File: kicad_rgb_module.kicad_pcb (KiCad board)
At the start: 2 copper layers, 25 x 25 mm, 41 parts, among them J1 Conn_HackConnect, SW1 TS-1088-AR02016, U1 STM32G030F6P6, U2 NCP114ASN330T1G

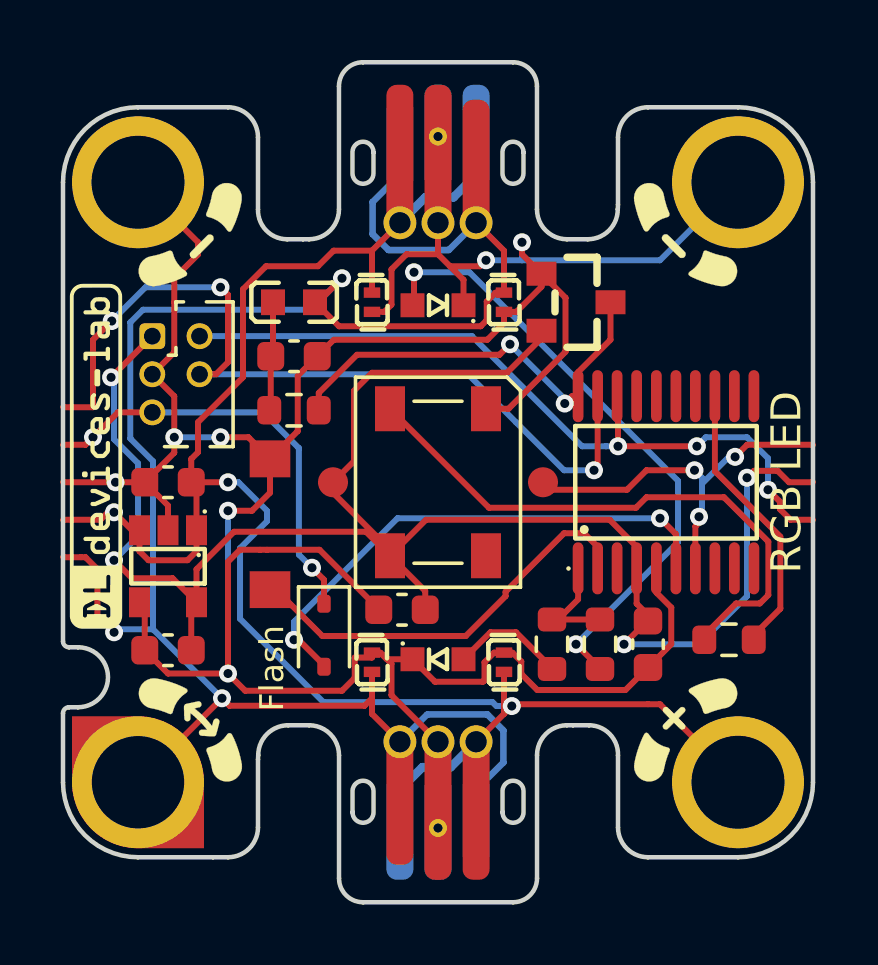
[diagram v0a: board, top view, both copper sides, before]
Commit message: Change BAT54 to BAS40-04 to reduce capacitance on JD_DATA
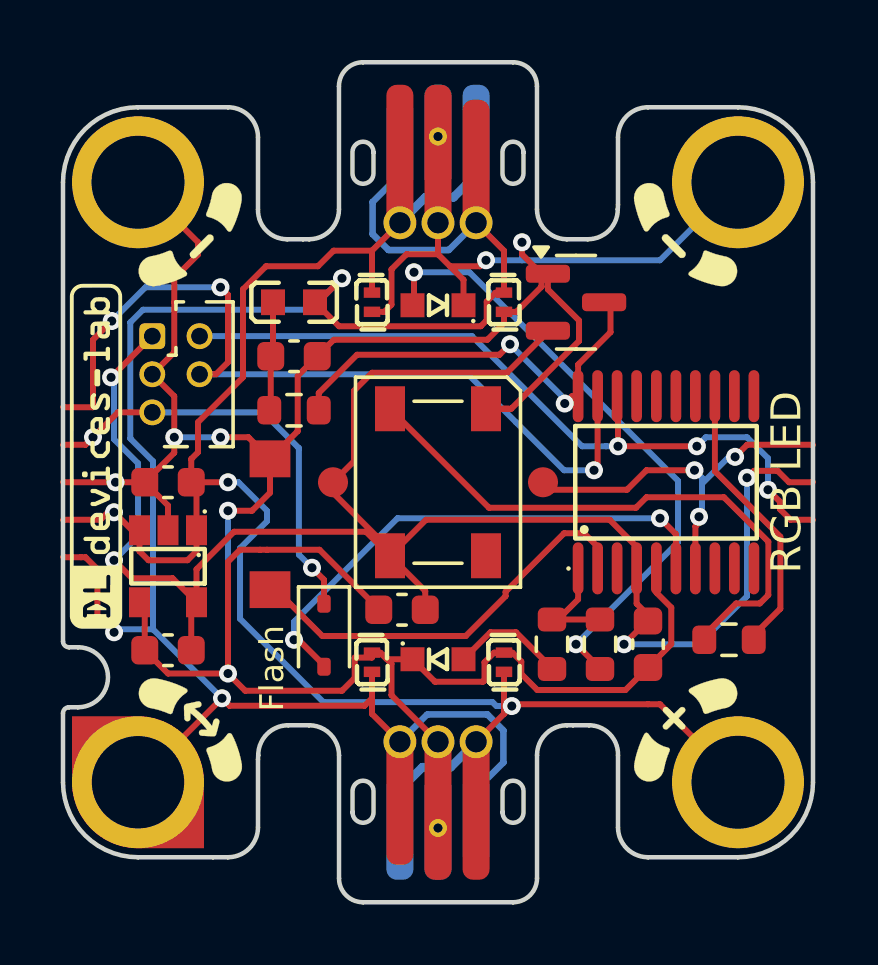
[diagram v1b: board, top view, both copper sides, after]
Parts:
- D1: value BAT54S -> BAS40-04; footprint Jacdac_Components:SOT-23_L2.9-W1.3-P1.90-LS2.4-BR -> Package_TO_SOT_SMD:SOT-23
- turned D1 to 0 degrees
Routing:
- net GND: track 108.5 -> 109.6 mm

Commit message: Remove GerberSockets to simplify the template, replace QR code with placeholder
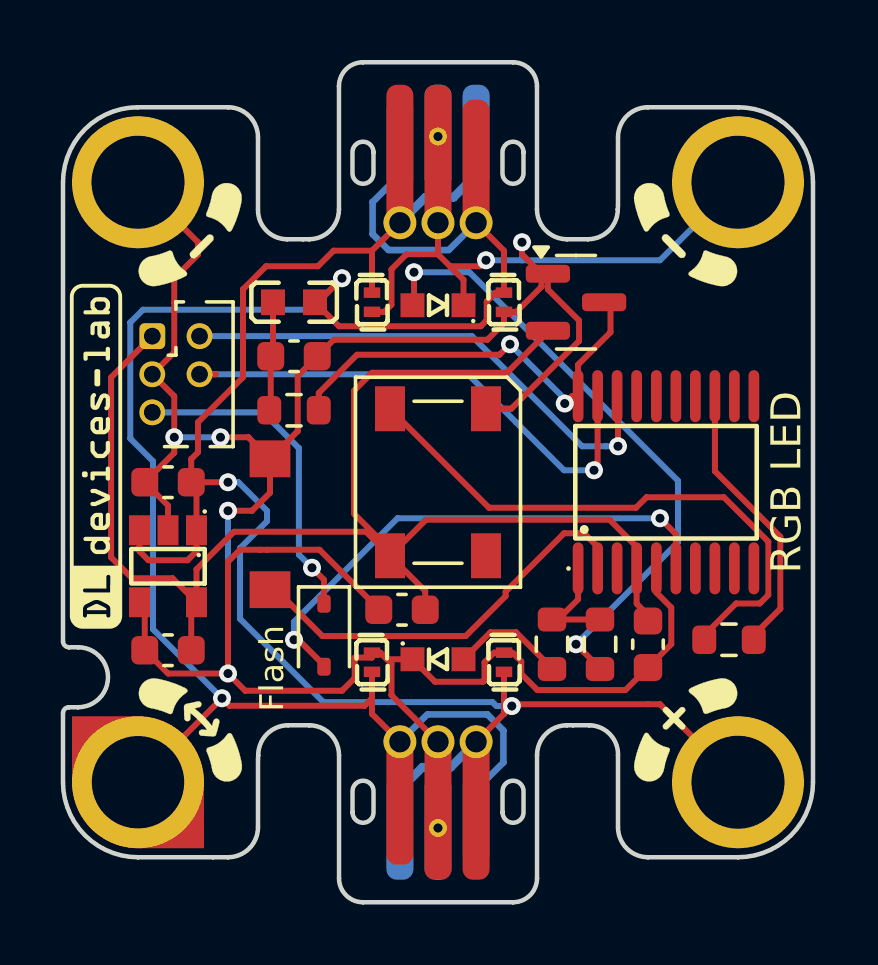
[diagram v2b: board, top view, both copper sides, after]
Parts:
- removed GS1: GND, GerberSockets:GND
- removed GS2: JD_DATA, GerberSockets:JD_DATA
- removed GS3: JD_PWR, GerberSockets:JD_PWR
- removed GS4: RESET, GerberSockets:RESET
- removed GS5: SWCLK, GerberSockets:SWCLK
- removed GS6: SWDIO~^, GerberSockets:SWDIO~^
- removed GS7: 3V3, GerberSockets:3V3
- removed GS8: SERIAL, GerberSockets:SERIAL
- removed TP1, TP2: TestPoint, Jacdac_Application:TestPoint_Pad_D1.0mm
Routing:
- net +3V3: track 62.4 -> 48.8 mm, vias 4 -> 0
- net /SERIAL: track 13.6 -> 0.00 mm, vias 3 -> 0
- net /SWCLK: track 28.9 -> 17.5 mm, vias 3 -> 1
- net /SWDIO: track 25.7 -> 17.2 mm, vias 3 -> 1
- net /JD_DATA: track 49.7 -> 44.8 mm, vias 3 -> 2
- net /nRESET-SAFE: track 14.3 -> 10.9 mm, vias 2 -> 1
- net GND: track 109.6 -> 106.9 mm, vias 7 -> 6
- net JD_PWR: track 51.7 -> 49.0 mm, vias 3 -> 2
